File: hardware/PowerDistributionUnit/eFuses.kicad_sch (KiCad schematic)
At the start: 13 parts, among them U3 TCA9544A, U36 MCP23S17-E/SS

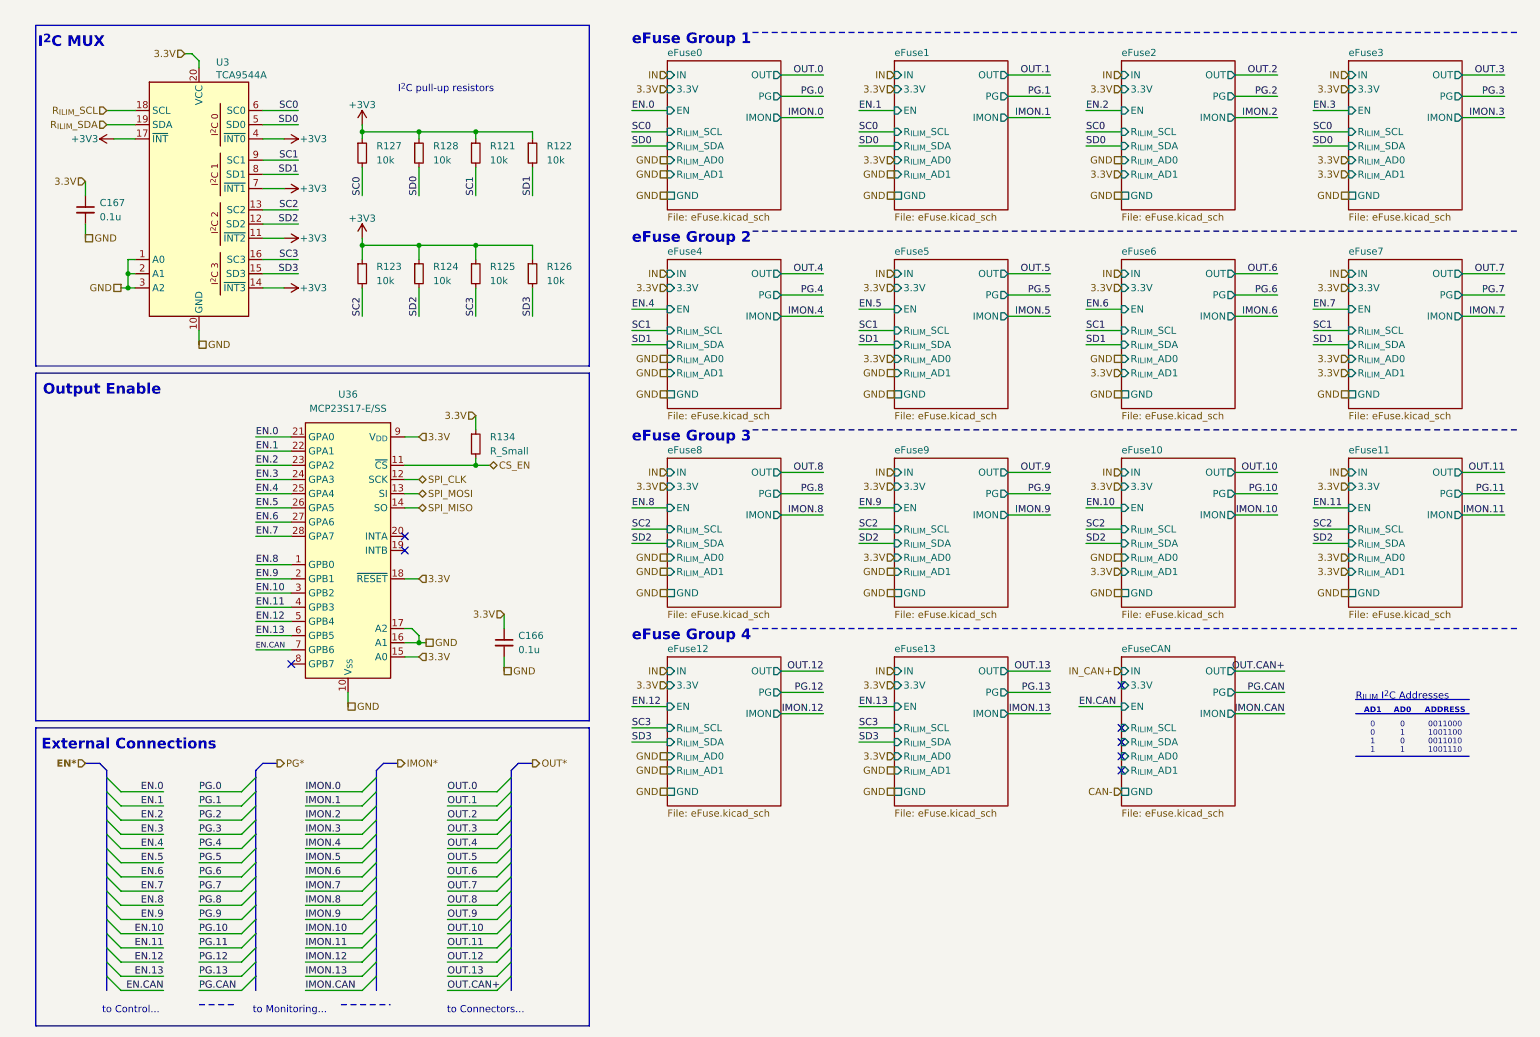
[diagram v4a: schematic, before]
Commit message: Continued revising eFuse isolation. Also fixed pulls on ADCMUX
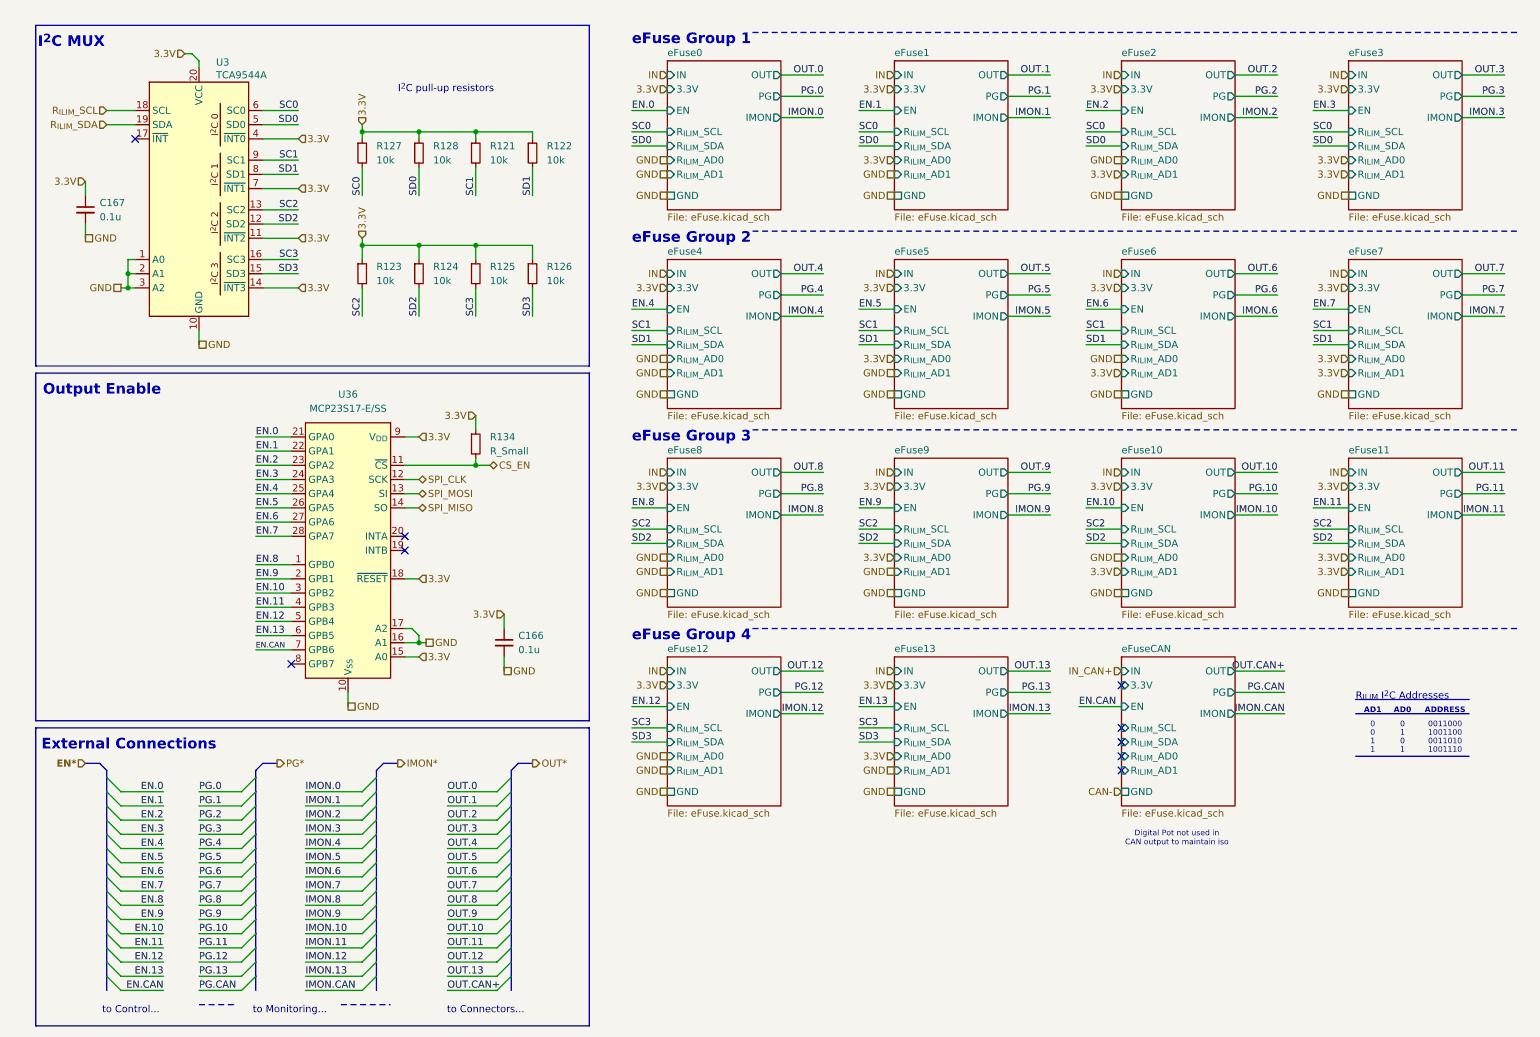
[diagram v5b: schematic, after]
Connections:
- net 3.3V: now also R121.1, R122.1, R123.1, R124.1, R125.1, R126.1, R127.1, R128.1, U3.11 (~{INT2}), U3.14 (~{INT3}), U3.4 (~{INT0}), U3.7 (~{INT1})
- removed net +3V3: R121.1, R122.1, R123.1, R124.1, R125.1, R126.1, R127.1, R128.1, U3.11 (~{INT2}), U3.14 (~{INT3}), U3.17 (~{INT}), U3.4 (~{INT0}), U3.7 (~{INT1})
- no-connect marks 8 -> 9
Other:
- note added: "Digital Pot not used in CAN output to maintain iso"

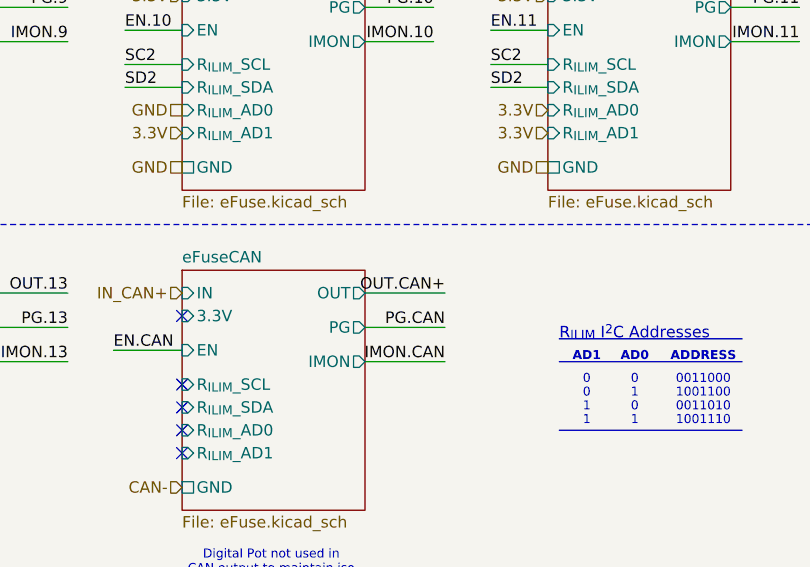
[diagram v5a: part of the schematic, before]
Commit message: Added footprints, added pull-up resistors, finished wiring up SOM
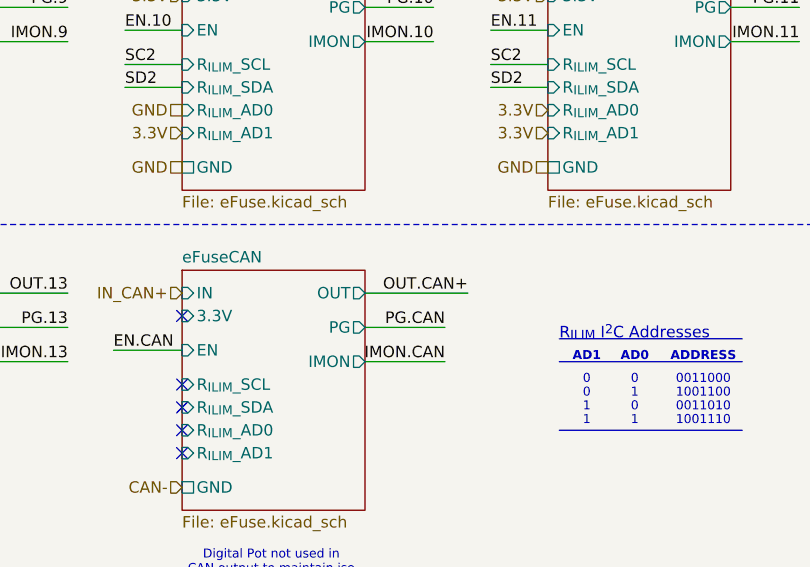
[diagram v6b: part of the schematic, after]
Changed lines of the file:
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@@
 	(wire
 		(pts
-			(xy 240.03 130.81) (xy 231.14 130.81)
+			(xy 242.57 130.81) (xy 231.14 130.81)
 		)
 		(stroke
@@
 	)
 	(label "OUT.CAN+"
-		(at 240.03 130.81 180)
-		(fields_autoplaced yes)
-		(effects
+		(at 242.57 130.81 180)
+		(fields_autoplaced yes)
+		(effects

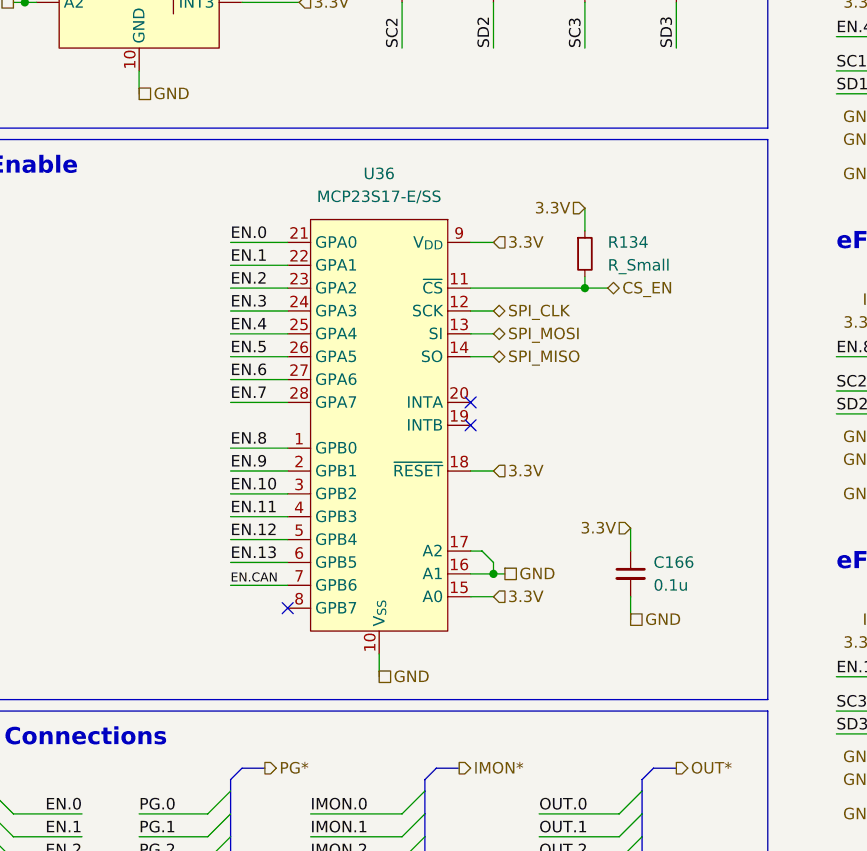
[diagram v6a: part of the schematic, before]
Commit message: Added non populated 0 ohm resistor
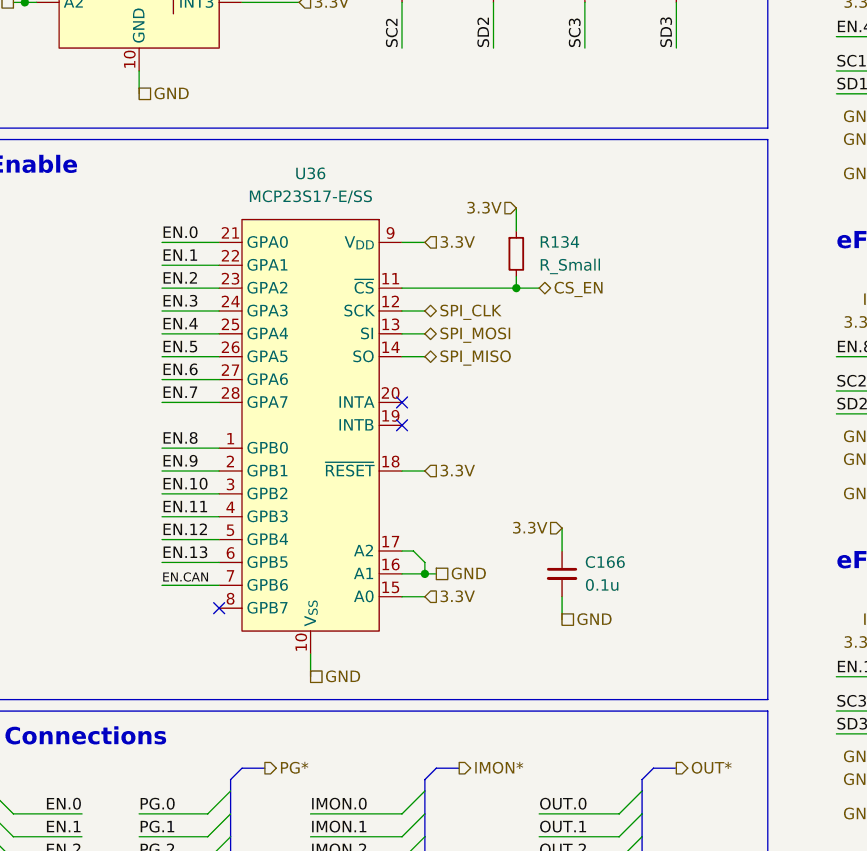
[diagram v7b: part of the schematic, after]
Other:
- moved on the sheet: C166, R134, U36

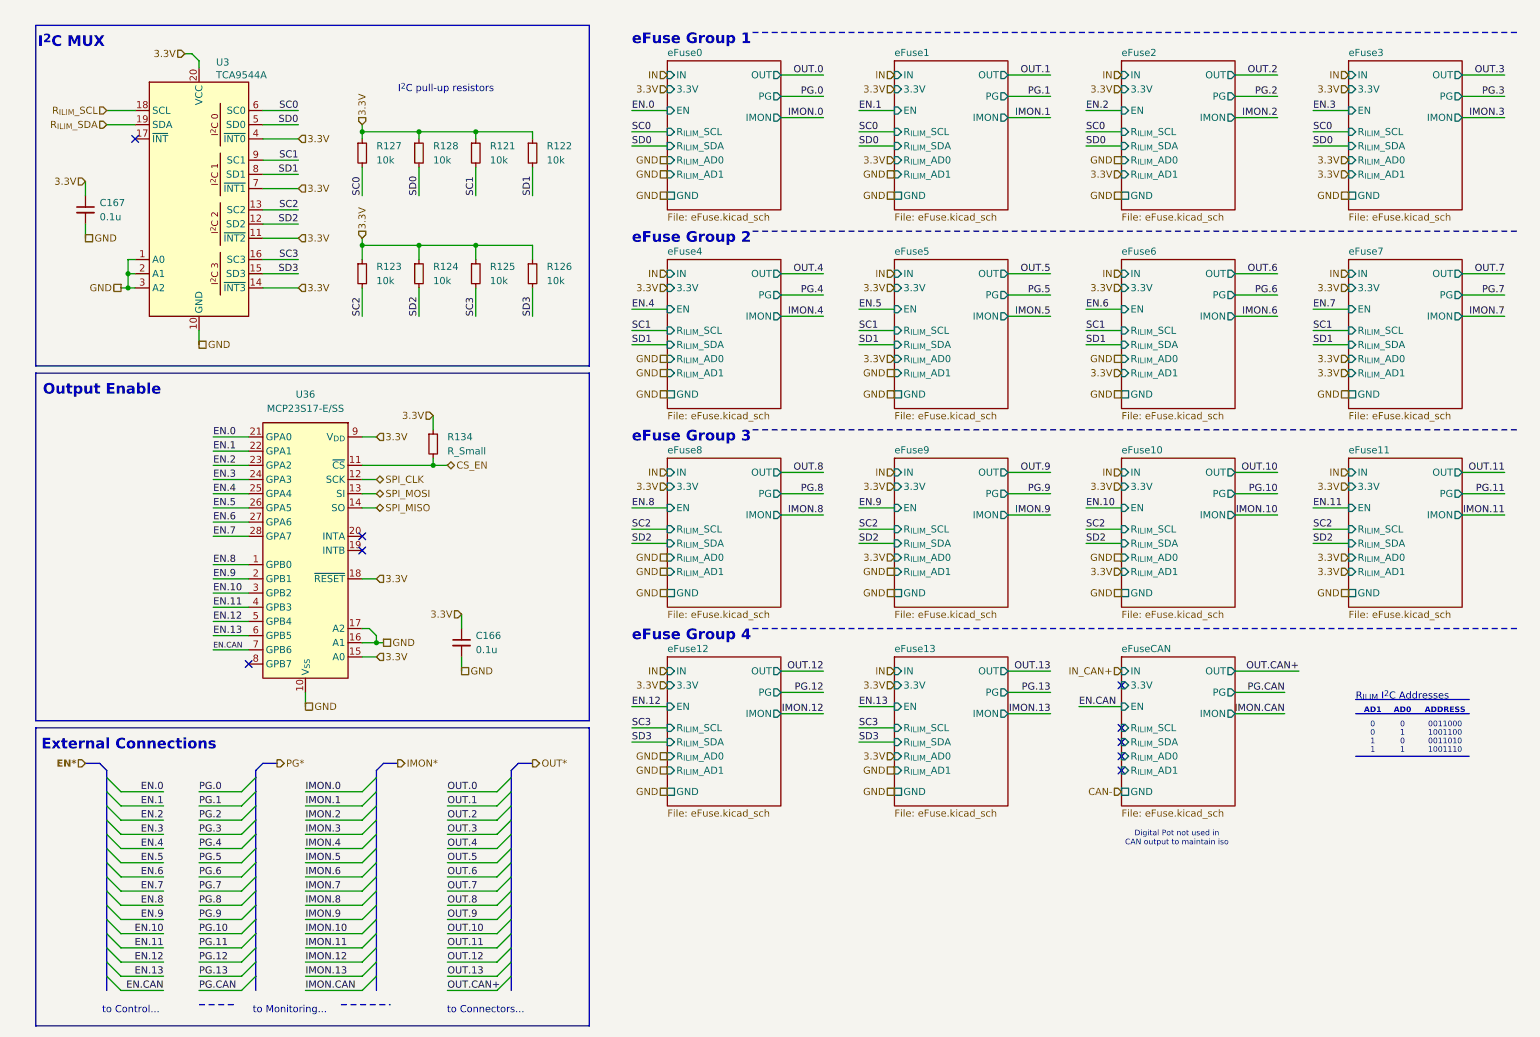
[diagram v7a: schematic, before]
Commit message: added gndpwr to separate from everything on gnd
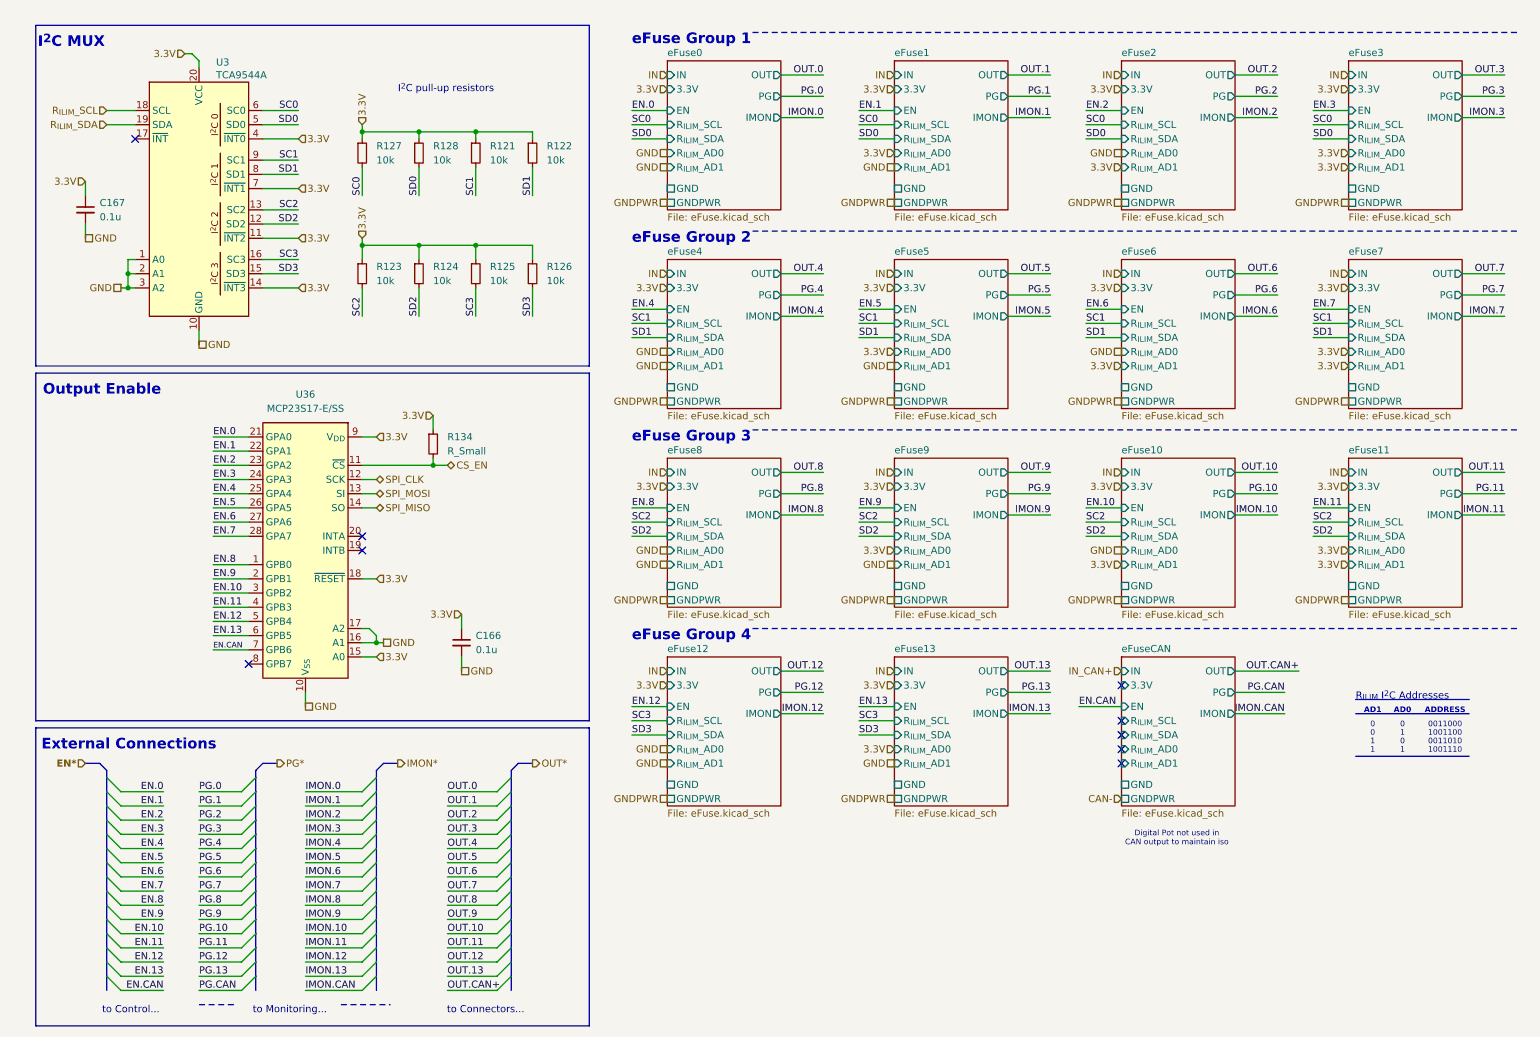
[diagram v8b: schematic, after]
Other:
- sheet eFuse0 ports: added GNDPWR; removed none
- sheet eFuse1 ports: added GNDPWR; removed none
- sheet eFuse10 ports: added GNDPWR; removed none
- sheet eFuse11 ports: added GNDPWR; removed none
- sheet eFuse12 ports: added GNDPWR; removed none
- sheet eFuse13 ports: added GNDPWR; removed none
- sheet eFuse2 ports: added GNDPWR; removed none
- sheet eFuse3 ports: added GNDPWR; removed none
- sheet eFuse4 ports: added GNDPWR; removed none
- sheet eFuse5 ports: added GNDPWR; removed none
- sheet eFuse6 ports: added GNDPWR; removed none
- sheet eFuse7 ports: added GNDPWR; removed none
- sheet eFuse8 ports: added GNDPWR; removed none
- sheet eFuse9 ports: added GNDPWR; removed none
- sheet eFuseCAN ports: added GNDPWR; removed none
